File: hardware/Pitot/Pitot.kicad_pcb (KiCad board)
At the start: 2 copper layers, 52.2 x 61.5 mm, 53 parts, among them IC1 ABPMRRV060MG2A3, IC2 ABPMRRV060MG2A3, J1 53307-2471, J3 MX150_02x06_Vertical, J4 Conn_01x07, U2 LDO40LPURY

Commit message: routing improved on pitot board
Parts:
- added +3.3MCU1: TestPoint, TestPoint:TestPoint_Pad_1.0x1.0mm, B.Cu at (93.5, 43.5)
- added C3: 10uf, Capacitor_SMD:C_0805_2012Metric_Pad1.18x1.45mm_HandSolder, F.Cu at (64.2, 80.8)
- added C4: 0.1uF, Capacitor_SMD:C_0603_1608Metric_Pad1.08x0.95mm_HandSolder, F.Cu at (63.0, 78.8)
- moved PressERR2 5.77 mm to (58.5, 82.8)
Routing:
- net GND: track 45.2 -> 49.8 mm, vias 15 -> 16
- net +3.3V: track 13.9 -> 16.3 mm
- net +3.3VMCU: track 13.1 -> 12.3 mm
- net /SCL1: vias 2 -> 3
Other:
- board text added: "Karthik Kurapati Revision A November 25"
- board text removed: "Karthik Kurapati Revision A Novemember 25"

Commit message: final pitot board + bom files
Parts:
- added ADJL1: TP5, TestPoint:TestPoint_Pad_D1.0mm, F.Cu at (90.5, 52.2)
- added EN1: TP2, TestPoint:TestPoint_Pad_D1.0mm, F.Cu at (96.2, 43.5)
- added GNDL1: TP6, TestPoint:TestPoint_Pad_D1.0mm, F.Cu at (99.5, 53.5)
- added VinL1: TP1, TestPoint:TestPoint_Pad_D1.0mm, F.Cu at (97.8, 46.5)
- added VoutL1: TP3, TestPoint:TestPoint_Pad_D1.0mm, F.Cu at (90.8, 47.8)
- added VsenseL1: TP4, TestPoint:TestPoint_Pad_D1.0mm, F.Cu at (90.8, 50.0)
- moved G*** 5.32 mm to (89.8, 83.8)
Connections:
- J4 pad 8: /pressERR_2 -> (no net)
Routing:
- net /SCL1: track 87.2 -> 72.3 mm
- net +24V: track 92.9 -> 97.8 mm, vias 8 -> 10
- net Net-(U2-Vout): track 27.7 -> 32.1 mm
- net GND: track 49.8 -> 52.8 mm
- net Net-(U2-ADJ): track 4.63 -> 7.37 mm
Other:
- board text added: "Karthik Kurapati November 25'"
- board text added: "pitot board rev a"
- board text removed: "Karthik Kurapati Revision A November 25"

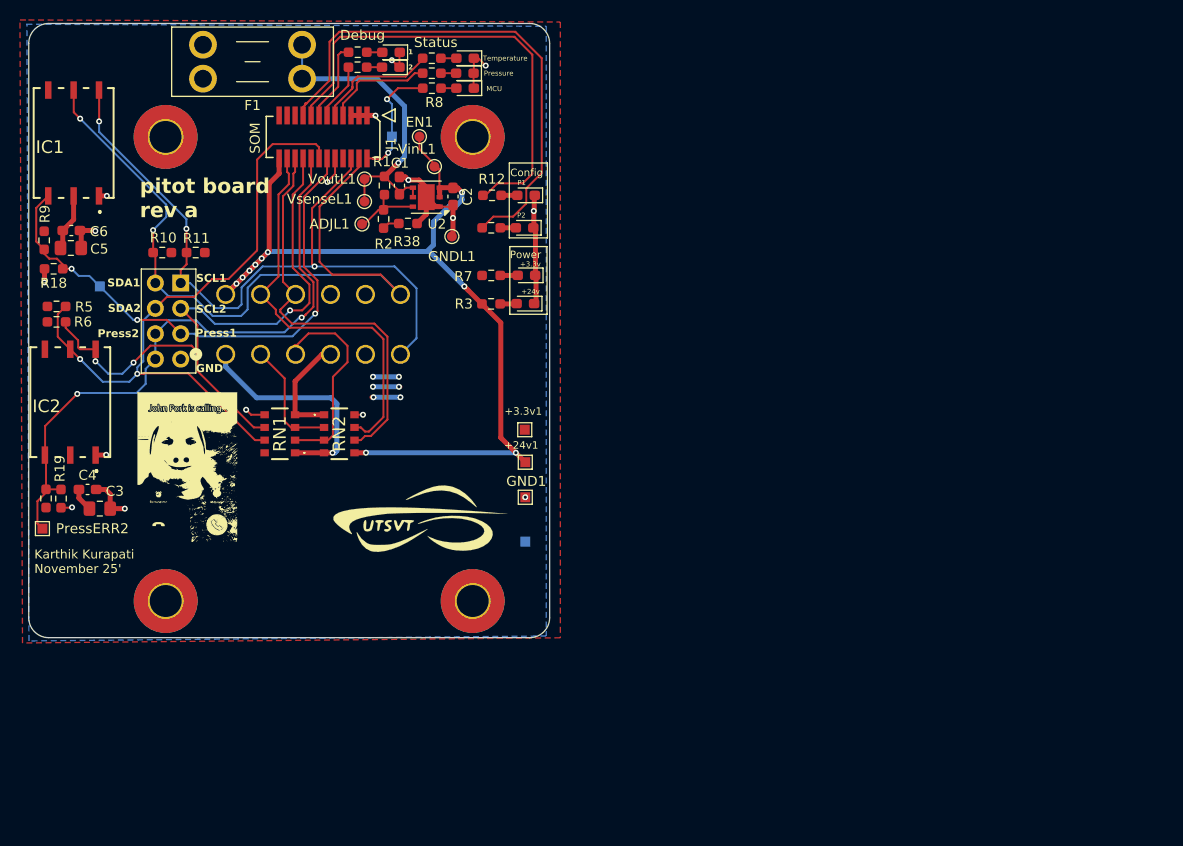
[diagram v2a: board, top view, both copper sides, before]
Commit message: small changes, mostly silkscreen to layout.
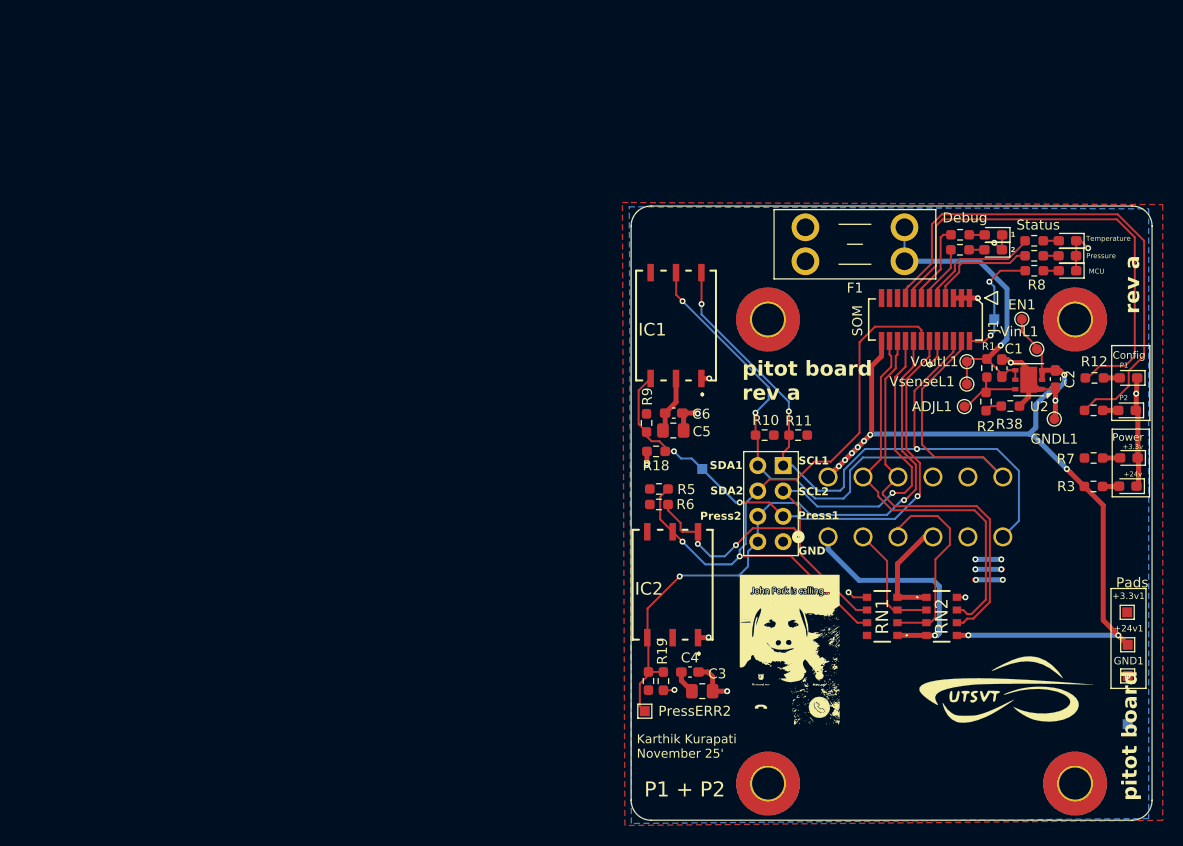
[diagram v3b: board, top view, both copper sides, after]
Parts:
- J4: value Conn_01x07 -> Conn_01x08
- moved +24v1 63.0 mm to (167.2, 94.4)
- moved GND2 63.0 mm to (167.2, 102.3)
- moved J3 63.0 mm to (137.2, 83.6)
- moved J4 63.0 mm to (132.7, 76.4)
- moved R11 63.0 mm to (134.2, 73.4)
- moved R2 63.0 mm to (153.0, 70.0)
- moved R38 63.0 mm to (155.4, 70.5)
- moved RN2 63.0 mm to (148.5, 91.5)
- moved +3.3v1 63.0 mm to (167.1, 91.1)
- moved C2 63.0 mm to (159.9, 67.8)
- moved C3 63.0 mm to (124.6, 99.0)
- moved D1 63.0 mm to (167.2, 78.5)
- moved D3 63.0 mm to (161.1, 56.9)
- moved D4 63.0 mm to (167.2, 67.7)
- moved D6 63.0 mm to (161.1, 55.4)
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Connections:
- J4 pad 8: (no net) -> /pressERR_2
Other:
- board text added: "P1 + P2"
- board text added: "Pads"
- board text added: "pitot board"
- board text added: "rev a"
